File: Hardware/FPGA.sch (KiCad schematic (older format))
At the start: 5 parts, among them U501 W25Q128JVxxM, U502 ICE40UP5K-SG48, U503 Crystal Oscillator

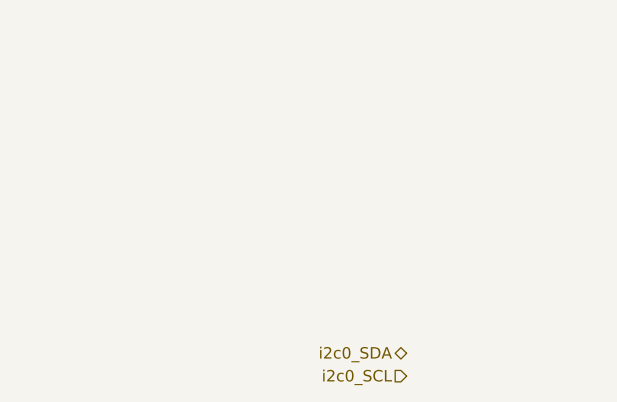
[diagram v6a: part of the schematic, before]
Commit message: Adding 2-DIP switch.
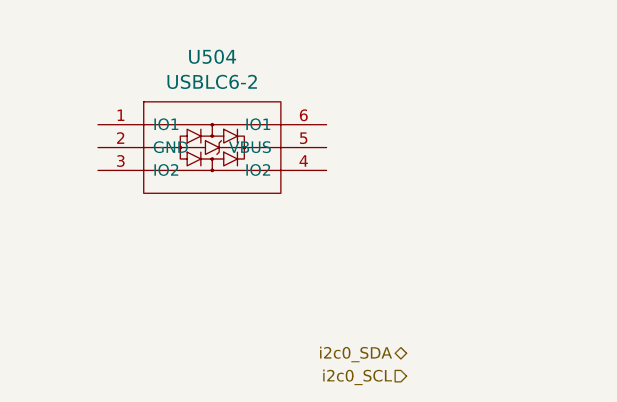
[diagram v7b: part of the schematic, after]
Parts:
- added U504: USBLC6-2, pkl_housings_sot:SOT-666, symbol pkl_misc:USBLC6-2
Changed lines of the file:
@@
 	-1   0    0    -1
 $EndComp
+$Comp
+L pkl_misc:USBLC6-2 U?
+U 1 1 612F1307
+P 2350 1500
+AR Path="/61291C71/612F1307" Ref="U?"  Part="1"
+AR Path="/612F1307" Ref="U?"  Part="1"
+AR Path="/611E3335/612F1307" Ref="U504"  Part="1"
+F 0 "U504" H 2350 1895 60  0000 C CNN
+F 1 "USBLC6-2" H 2350 1785 60  0000 C CNN
+F 2 "pkl_housings_sot:SOT-666" H 2350 1785 60  0001 C CNN
+F 3 "https://www.farnell.com/datasheets/1738051.pdf" H 2350 1500 60  0001 C CNN
+F 4 "tvs-diode-sot666" H 2350 1500 50  0001 C CNN "Key"
+F 5 "E14" H 2350 1500 50  0001 C CNN "Source"
+F 6 "USBLC6-2SC6" H 2350 1500 50  0001 C CNN "MPN"
+F 7 "1269406" H 2350 1500 50  0001 C CNN "E14PN"
+	1    2350 1500
+	1    0    0    -1
+$EndComp
 $EndSCHEMATC

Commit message: Adding some connectivity.
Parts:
- removed C501: 0201, 100nF, 10V, X5R, 20%, tomu-fpga:C_0201_0603Metric, symbol Device:C_Small
- removed JP501: Jumper, pkl_jumpers:J_NC_0402_15, symbol pkl_misc:pkl_jumper_nc
- added C? (x2): 0.1uF, Capacitor_SMD:C_0603_1608Metric, symbol Device:C_Small
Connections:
- net labels added: BTN_1, BTN_2, DIP_1, DIP_2, ~FLASH_CS
- net labels removed: FLASH_~CS, SPI_~CS
- wire segments 33 -> 23
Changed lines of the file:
@@
 NoConn ~ 9650 2750
 Wire Wire Line
-	9300 2950 9300 2550
-Wire Wire Line
 	10650 2400 10650 2750
-Wire Wire Line
-	8750 2950 9300 2950
-Text Label 9200 2950 2    50   ~ 0
+Text Label 9550 2550 2    50   ~ 0
 OSC_IN
-Wire Wire Line
-	9650 2550 9300 2550
-Wire Wire Line
-	10450 2750 10350 2750
-Wire Wire Line
-	10450 2550 10550 2550
-$Comp
-L Device:C_Small C501
-U 1 1 614FF0DF
-P 10450 2650
-F 0 "C501" H 10500 2700 50  0000 L CNN
-F 1 "0201, 100nF, 10V, X5R, 20%" H 10300 2450 50  0000 L CNN
-F 2 "tomu-fpga:C_0201_0603Metric" H 10450 2650 50  0001 C CNN
-F 3 "" H 10450 2650 50  0001 C CNN
-F 4 "ANY" H 5400 550 50  0001 C CNN "MPN"
-F 5 "ANY" H 5400 550 50  0001 C CNN "MYPN"
-F 6 "ANY" H 5400 550 50  0001 C CNN "Manufacturer"
-F 7 "C" H 10450 2650 50  0001 C CNN "Spice_Primitive"
-F 8 "100n" H 10450 2650 50  0001 C CNN "Spice_Model"
-F 9 "Y" H 10450 2650 50  0001 C CNN "Spice_Netlist_Enabled"
-	1    10450 2650
-	-1   0    0    -1
-$EndComp
 Wire Wire Line
 	10550 2550 10550 2850
@@
 	-1   0    0    -1
 $EndComp
-Connection ~ 10450 2550
-Wire Wire Line
-	10350 2550 10450 2550
-Connection ~ 10450 2750
-Wire Wire Line
-	10650 2750 10450 2750
 $Comp
 L power:+3V3 #PWR0502
@@
 P 10000 2500
 F 0 "U503" H 9750 2450 50  0000 C CNN
-F 1 "Crystal Oscillator" H 10150 2450 50  0000 C CNN
+F 1 "Crystal Oscillator" H 10250 2450 50  0000 C CNN
 F 2 "tomu-fpga:XTAL-2520" H 10000 2500 50  0001 C CNN
 F 3 "https://www.ecsxtal.com/store/pdf/ECS-2520MV.pdf" H 10000 2500 50  0001 C CNN
@@
 	1    0    0    1
 $EndComp
-Text Label 4450 6100 0    50   ~ 0
-SPI_~CS
 Text Label 3700 6200 0    50   ~ 0
 SPI_SCK
@@
 Text Label 3700 6600 0    50   ~ 0
 SPI_~HLD~-IO3
-Wire Wire Line
-	3000 6400 3300 6400
-Wire Wire Line
-	3000 6300 3400 6300
-$Comp
-L pkl_misc:pkl_jumper_nc JP?
-U 1 1 612A0D70
-P 4250 6100
-AR Path="/61291C71/612A0D70" Ref="JP?"  Part="1"
-AR Path="/611E3335/612A0D70" Ref="JP501"  Part="1"
-F 0 "JP501" H 4250 6200 50  0000 C CNN
-F 1 "Jumper" H 4250 6245 60  0001 C CNN
-F 2 "pkl_jumpers:J_NC_0402_15" H 4250 6100 60  0001 C CNN
-F 3 "" H 4250 6100 60  0000 C CNN
-F 4 "ANY" H 4250 6100 50  0001 C CNN "Source"
-	1    4250 6100
-	1    0    0    -1
-$EndComp
-Wire Wire Line
-	3000 6100 3600 6100
-Wire Wire Line
-	3000 6200 3500 6200
-Wire Wire Line
-	3000 6500 3200 6500
-Wire Wire Line
-	3000 6600 3100 6600
-Wire Wire Line
-	3100 5700 3100 6600
-Connection ~ 3100 6600
-Wire Wire Line
-	3200 5600 3200 6500
-Connection ~ 3200 6500
-Wire Wire Line
-	3500 5300 3500 6200
-Connection ~ 3500 6200
-Wire Wire Line
-	3600 5000 3600 6100
-Wire Wire Line
-	3600 6100 4150 6100
-Wire Wire Line
-	3400 5400 3400 6300
-Connection ~ 3400 6300
-Wire Wire Line
-	3300 5500 3300 6400
-Connection ~ 3300 6400
 Text Label 3700 6100 0    50   ~ 0
-FLASH_~CS
-Wire Wire Line
-	3500 6200 3700 6200
-Wire Wire Line
-	4350 6100 4450 6100
-Wire Wire Line
-	3400 6300 3700 6300
-Wire Wire Line
-	3300 6400 3700 6400
-Wire Wire Line
-	3200 6500 3700 6500
-Wire Wire Line
-	3100 6600 3700 6600
-Connection ~ 3600 6100
-Wire Wire Line
-	1500 6600 1800 6600
+~FLASH_CS
 Wire Wire Line
 	1700 6100 1800 6100
@@
 	1    0    0    -1
 $EndComp
+Text HLabel 3250 4100 0    50   Output ~ 0
+BTN_2
+Text HLabel 3250 3950 0    50   Output ~ 0
+BTN_1
+Text HLabel 3250 4550 0    50   Output ~ 0
+DIP_2
+Text HLabel 3250 4400 0    50   Output ~ 0
+DIP_1
+Wire Wire Line
+	3000 6500 3700 6500
+Wire Wire Line
+	3000 6200 3700 6200
+Wire Wire Line
+	3000 6100 3700 6100
+Wire Wire Line
+	3000 6300 3700 6300
+Wire Wire Line
+	3000 6400 3700 6400
+Wire Wire Line
+	3000 6600 3700 6600
+Connection ~ 9650 2550
+Wire Wire Line
+	9650 2550 9700 2550
+Wire Wire Line
+	9550 2550 9650 2550
+$Comp
+L Device:C_Small C?
+U 1 1 61350B96
+P 10450 2650
+AR Path="/611E335F/61350B96" Ref="C?"  Part="1"
+AR Path="/611E3335/61350B96" Ref="C?"  Part="1"
+F 0 "C?" H 10565 2832 50  0000 L CNN
+F 1 "0.1uF" H 10565 2741 50  0000 L CNN
+F 2 "Capacitor_SMD:C_0603_1608Metric" H 10488 2500 50  0001 C CNN
+F 3 "~" H 10450 2650 50  0001 C CNN
+F 4 "C0603C104K5RACAUTO" H 10450 2650 50  0001 C CNN "MPN"
+F 5 "399-6856-1-ND" H 10450 2650 50  0001 C CNN "DPN"
+F 6 "50V" H 10565 2650 50  0000 L CNN "Tol"
+F 7 "0603" H 10565 2559 50  0000 L CNN "Pkg"
+F 8 "X7R" H 10565 2468 50  0000 L CNN "TCoff"
+	1    10450 2650
+	1    0    0    -1
+$EndComp
+Wire Wire Line
+	10350 2550 10450 2550
+Wire Wire Line
+	10350 2750 10450 2750
+Connection ~ 10450 2550
+Wire Wire Line
+	10450 2550 10550 2550
+Connection ~ 10450 2750
+Wire Wire Line
+	10450 2750 10650 2750
+$Comp
+L power:GND #PWR?
+U 1 1 613565CE
+P 1700 6700
+F 0 "#PWR?" H 1700 6450 50  0001 C CNN
+F 1 "GND" H 1705 6527 50  0000 C CNN
+F 2 "" H 1700 6700 50  0001 C CNN
+F 3 "" H 1700 6700 50  0001 C CNN
+	1    1700 6700
+	-1   0    0    -1
+$EndComp
+Wire Wire Line
+	1700 6600 1700 6700
+Wire Wire Line
+	1700 5900 1700 6100
+$Comp
+L power:+3V3 #PWR?
+U 1 1 6135A9D4
+P 1700 5900
+F 0 "#PWR?" H 1700 5750 50  0001 C CNN
+F 1 "+3V3" H 1715 6073 50  0000 C CNN
+F 2 "" H 1700 5900 50  0001 C CNN
+F 3 "" H 1700 5900 50  0001 C CNN
+	1    1700 5900
+	1    0    0    -1
+$EndComp
+$Comp
+L Device:C_Small C?
+U 1 1 6135A9DF
+P 1700 6350
+AR Path="/611E335F/6135A9DF" Ref="C?"  Part="1"
+AR Path="/611E3335/6135A9DF" Ref="C?"  Part="1"
+F 0 "C?" H 1815 6532 50  0000 L CNN
+F 1 "0.1uF" H 1815 6441 50  0000 L CNN
+F 2 "Capacitor_SMD:C_0603_1608Metric" H 1738 6200 50  0001 C CNN
+F 3 "~" H 1700 6350 50  0001 C CNN
+F 4 "C0603C104K5RACAUTO" H 1700 6350 50  0001 C CNN "MPN"
+F 5 "399-6856-1-ND" H 1700 6350 50  0001 C CNN "DPN"
+F 6 "50V" H 1815 6350 50  0000 L CNN "Tol"
+F 7 "0603" H 1815 6259 50  0000 L CNN "Pkg"
+F 8 "X7R" H 1815 6168 50  0000 L CNN "TCoff"
+	1    1700 6350
+	-1   0    0    -1
+$EndComp
+Wire Wire Line
+	1700 6100 1700 6250
+Connection ~ 1700 6100
+Wire Wire Line
+	1700 6450 1700 6600
+Connection ~ 1700 6600
+Wire Wire Line
+	1700 6600 1800 6600
 $EndSCHEMATC
